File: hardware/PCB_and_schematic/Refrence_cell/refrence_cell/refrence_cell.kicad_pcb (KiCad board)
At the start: 2 copper layers, 99 x 99 mm, 119 parts, among them J1 ICP_DEBUG, J11 R-Shunt, J12 BATT_IN, J13 BATT_OUT, J14 batt-24V-balancer, J15 pwm-12v-local, J2 DS18B20, J3 DS18B20, J4 DS18B20, J5 RS485, J6 Conn_01x02, J7 Conn_01x02, J8 RS485, Q1 BC817, Q2 BC327, Q3 BC337, Q4 IRF540N, Q5 IRF540N, U1 PIC16F886-IP, U2 TL431LP, U3 ST485, U4 LM358, U5 MP1584-Step-Down, U6 FAN7382, U7 NE555D, U8 FAN7382, U9 NE555D

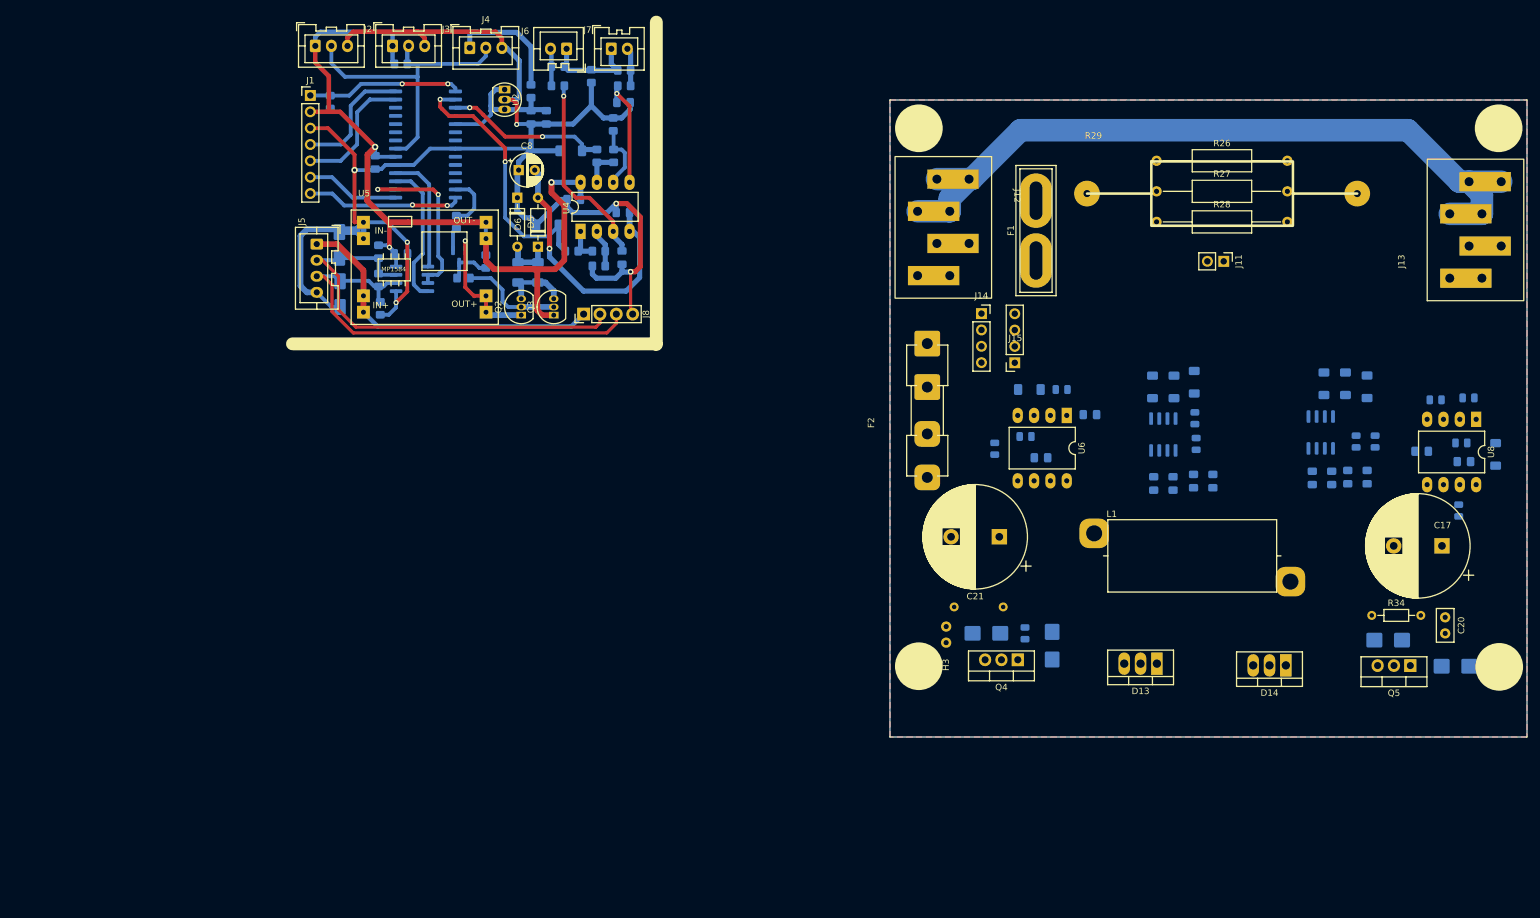
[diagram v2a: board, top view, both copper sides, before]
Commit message: routing power module
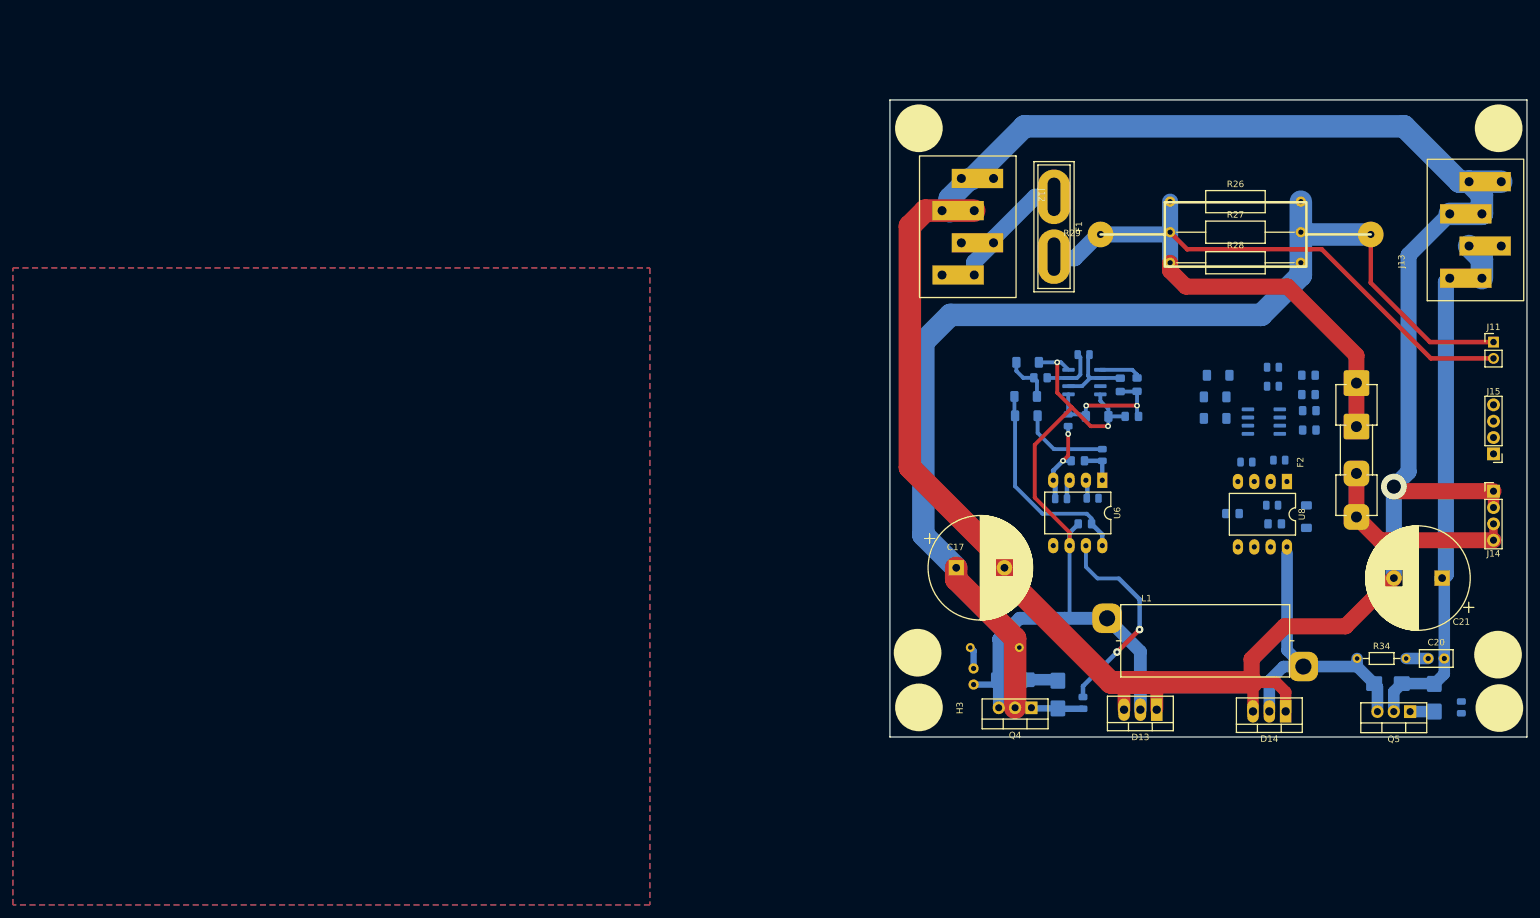
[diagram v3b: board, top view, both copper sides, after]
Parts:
- removed C1, C10, C2, C3, C4, C5, C9: 100n, Capacitor_SMD:C_0805_2012Metric_Pad1.18x1.45mm_HandSolder
- removed C11: 1u, Capacitor_SMD:C_0805_2012Metric_Pad1.18x1.45mm_HandSolder
- removed C6, C7: 10u, Capacitor_SMD:C_1206_3216Metric_Pad1.33x1.80mm_HandSolder
- removed C8: 100u, Capacitor_THT:CP_Radial_D5.0mm_P2.50mm
- removed D1, D2: D_TVS, Diode_SMD:D_SMA
- removed D3, D4: LL4148, Diode_SMD:D_MiniMELF
- removed D5, D6: LL4148, Diode_THT:D_DO-35_SOD27_P7.62mm_Horizontal
- removed J1: ICP_DEBUG, Connector_PinHeader_2.54mm:PinHeader_1x07_P2.54mm_Vertical
- removed J2, J3, J4: DS18B20, Connector_JST:JST_XA_B03B-XASK-1_1x03_P2.50mm_Vertical
- removed J5: RS485, Connector_JST:JST_XA_B04B-XASK-1_1x04_P2.50mm_Vertical
- removed J6, J7: Conn_01x02, Connector_JST:JST_XA_B02B-XASK-1_1x02_P2.50mm_Vertical
- removed J8: RS485, My-Footprints-connectors:PinHeader_1x04_P2.54mm_Vertical_littleBigger
- removed Q1: BC817, Package_TO_SOT_SMD:SOT-23
- removed Q2: BC327, Package_TO_SOT_THT:TO-92_Inline
- removed Q3: BC337, Package_TO_SOT_THT:TO-92_Inline
- removed R1, R14, R18, R20: 10k, Resistor_SMD:R_0805_2012Metric_Pad1.20x1.40mm_HandSolder
- removed R10, R11, R12, R13, R15, R17, R19, R2, R8: 1k, Resistor_SMD:R_0805_2012Metric_Pad1.20x1.40mm_HandSolder
- removed R16, R3, R5: 1K, Resistor_SMD:R_0805_2012Metric_Pad1.20x1.40mm_HandSolder
- removed R4: 120R, Resistor_SMD:R_0805_2012Metric_Pad1.20x1.40mm_HandSolder
- removed R6, R9: 1R, Resistor_SMD:R_0805_2012Metric_Pad1.20x1.40mm_HandSolder
- removed R7: 0R, Resistor_SMD:R_0805_2012Metric_Pad1.20x1.40mm_HandSolder
- removed U1: PIC16F886-IP, Package_SO:SOIC-28W_7.5x17.9mm_P1.27mm
- removed U2: TL431LP, My-Footprints:TO-92_Inline_LITTLE_BIGGER
- removed U3: ST485, Package_SO:SOIC-8_3.9x4.9mm_P1.27mm
- removed U4: LM358, Package_DIP:DIP-8_W7.62mm_LongPads
- removed U5: MP1584-Step-Down, My-Footprints-converters-modules:MP1584_Mini_3A_Step_Down_Conv
- added H5: MountingHole, My-Footprints:Mount-Hole-3mm, F.Cu at (18.3, 136.9)
- added H6: MountingHole, My-Footprints:Mount-Hole-3mm, F.Cu at (108.5, 137.2)
- J14, J15: footprint Connector_PinSocket_2.54mm:PinSocket_1x04_P2.54mm_Vertical -> My-Footprints-connectors:PinHeader_1x04_P2.54mm_Vertical_littleBigger
- moved J14 84.2 mm to (107.8, 111.8)
- moved J15 75.7 mm to (107.8, 106.0)
- moved C17 75.6 mm to (24.3, 123.7), turned to 0 degrees
- moved C21 69.1 mm to (99.8, 125.3)
- moved F2 67.0 mm to (86.5, 115.8)
- moved J11 43.8 mm to (107.8, 88.6), turned to 0 degrees
- moved C22 31.0 mm to (67.2, 115.3)
- moved C25 31.0 mm to (73.8, 116.9)
- moved D19 31.0 mm to (78.7, 115.8)
- moved R36 31.0 mm to (74.5, 107.0)
- moved U8 31.0 mm to (75.7, 110.3)
- moved R37 31.0 mm to (69.4, 107.3)
- moved R38 31.0 mm to (73.4, 114.0)
- moved R35 30.6 mm to (102.8, 145.4)
- moved C13 24.1 mm to (37.4, 94.2), turned to 180 degrees
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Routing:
- net R_shunt_L: track 0.00 -> 260.4 mm
- net GND: track 271.4 -> 13.7 mm, vias 7 -> 2
- net GNDA: track 131.4 -> 366.2 mm, vias 0 -> 1
- net +5V: track 181.7 -> 0.00 mm, vias 3 -> 0
- net R_shunt_H: track 0.00 -> 134.4 mm
- net Net-(D10-K): track 0.00 -> 120.1 mm, vias 0 -> 2
- net Net-(D15-A1): track 0.00 -> 80.1 mm
- net /Reference Cell/RS485_A: track 70.4 -> 0.00 mm
- net /Reference Cell/RS485_B: track 68.9 -> 0.00 mm
- net +24V: track 51.4 -> 0.00 mm
- net DS18B20_DATA: track 51.0 -> 0.00 mm
- net Net-(D14-A): track 0.00 -> 47.6 mm
- net -2V5: track 42.6 -> 0.00 mm, vias 1 -> 0
- net ADC_CELL_1: track 42.0 -> 0.00 mm, vias 2 -> 0
- net Net-(D7-K): track 0.00 -> 32.9 mm
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
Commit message: update power pcb
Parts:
- moved C23 19.9 mm to (61.5, 93.2), turned to 180 degrees
- moved R41 16.6 mm to (64.0, 106.2), turned to 90 degrees
- moved C27 9.73 mm to (77.5, 103.4), turned to 180 degrees
- moved D20 7.38 mm to (64.0, 101.1), turned to -90 degrees
- moved R38 5.53 mm to (77.5, 110.2)
- moved C26 4.35 mm to (77.5, 100.8), turned to 180 degrees
- moved D17 4.13 mm to (60.5, 101.1), turned to 90 degrees
- moved R39 3.42 mm to (70.4, 96.8), turned to 180 degrees
- moved D18 2.47 mm to (62.2, 96.3)
- moved R36 2.13 mm to (72.4, 107.2)
- moved R37 2.09 mm to (67.3, 107.2)
- moved C24 1.97 mm to (77.5, 98.3), turned to 180 degrees
- moved U8 1.82 mm to (73.9, 110.3)
- moved C25 1.82 mm to (72.0, 116.9)
- moved U9 1.82 mm to (70.3, 101.0)
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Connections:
- R36 pad 2: PWM_OUT_DISCH -> PWM_OUT_CHRG
- U8 pad 2: PWM_OUT_DISCH -> PWM_OUT_CHRG
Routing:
- net GND: track 13.7 -> 120.1 mm, vias 2 -> 3
- net PWM_OUT_CHRG: track 0.00 -> 96.4 mm, vias 0 -> 2
- net GNDA: track 366.2 -> 457.3 mm
- net PWM_OUT_DISCH: track 2.94 -> 89.5 mm
- net +12V_LOCAL: track 5.78 -> 76.7 mm, vias 0 -> 1
- net Net-(D14-A): track 47.6 -> 105.6 mm, vias 0 -> 2
- net Net-(U8-HO): track 0.00 -> 51.7 mm, vias 0 -> 2
- net Net-(D17-K): track 0.00 -> 38.6 mm, vias 0 -> 2
- net +5V: track 0.00 -> 32.5 mm, vias 0 -> 4
- net R_shunt_H: track 134.4 -> 163.5 mm
- net Net-(D20-A): track 0.00 -> 24.6 mm
- net Net-(J12-Pin_3): track 19.0 -> 38.0 mm
- net Net-(U9-Q): track 0.00 -> 14.1 mm
- net Net-(U9-THR): track 0.00 -> 13.0 mm
- net Net-(D15-A1): track 80.1 -> 86.8 mm
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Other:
- board text added: "+12V_LOCAL"
- board text added: "+BATT_24V"
- board text added: "GND"
- board text added: "GND_A"
- board text added: "PWM_OUT_CHRG"
- board text added: "PWM_OUT_DISCH"
- board text added: "R_SHUNT_H"
- board text added: "R_SHUNT_L"
